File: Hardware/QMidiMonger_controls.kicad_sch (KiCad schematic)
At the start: 26 parts, among them J1 CV_Out, J2 CV_Out, J20 Conn_01x09_Female, J21 Conn_01x08_Female, J22 Conn_01x08_Female, J23 Conn_01x03_Female, J3 CV_Out, J4 Gate_Out, J5 Gate_Out, J6 Gate_Out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

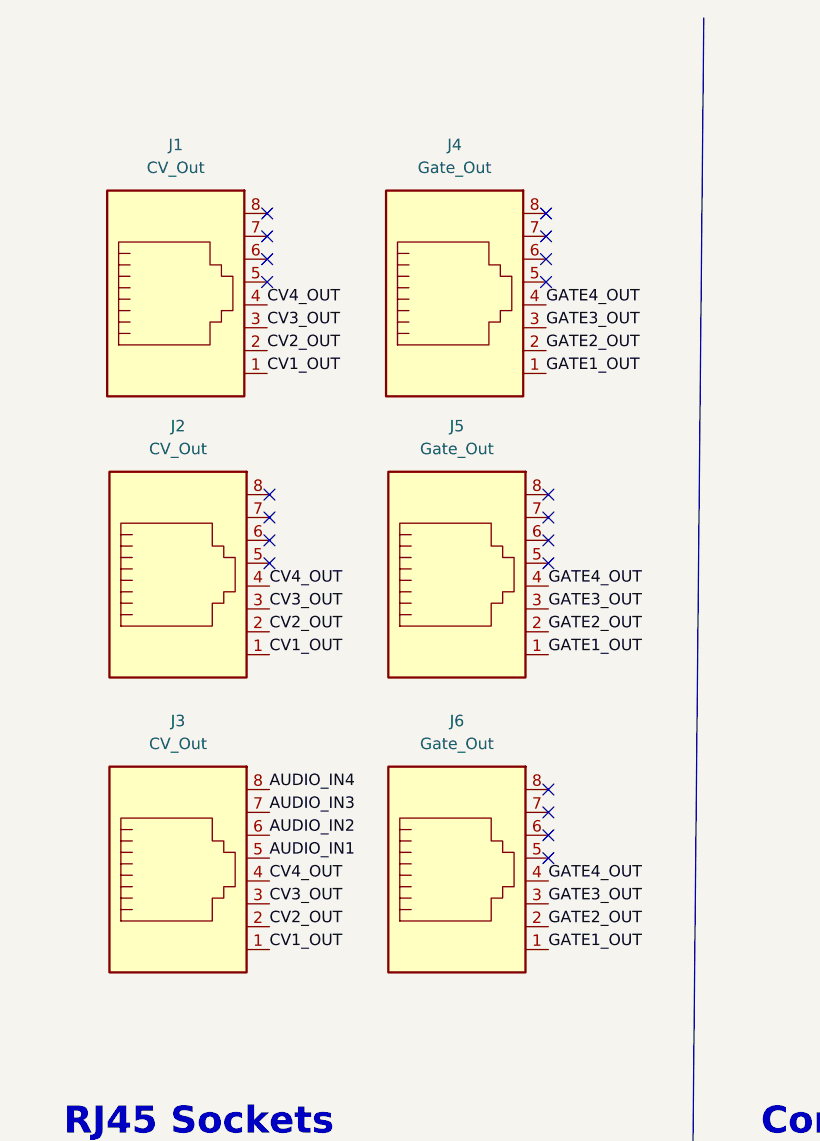
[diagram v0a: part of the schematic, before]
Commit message: Normalised audio to all CV returns
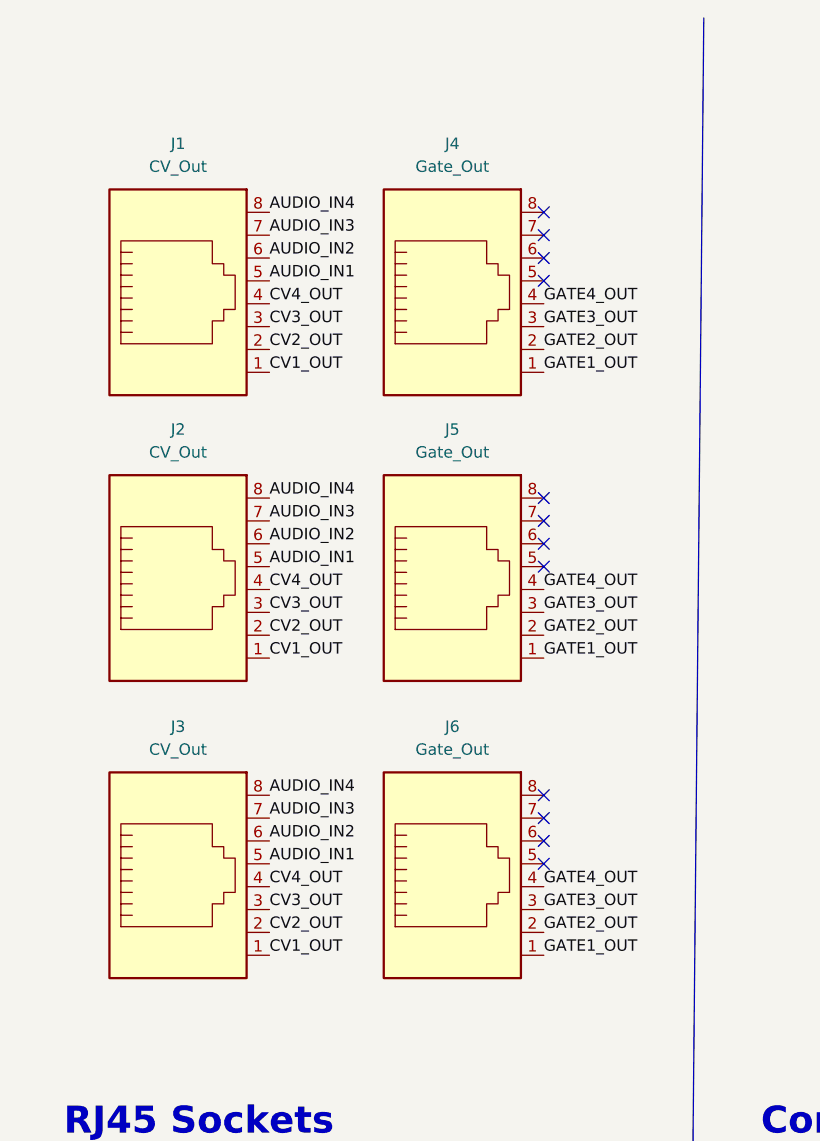
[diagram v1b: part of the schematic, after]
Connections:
- net AUDIO_IN1: now also J1.5, J2.5
- net AUDIO_IN2: now also J1.6, J2.6
- net AUDIO_IN3: now also J1.7, J2.7
- net AUDIO_IN4: now also J1.8, J2.8
- no-connect marks 20 -> 12
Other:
- moved on the sheet: J3, J5, J6
